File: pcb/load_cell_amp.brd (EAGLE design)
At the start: 50.5 x 30.5 mm, 6 parts, among them IC2 INA122P, J1 LOAD_CELL, J2 G29

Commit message: renamed IC2 to IC1
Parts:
- moved R_REF 1.65 mm to (58.0, 40.6)
- renumbered IC2 to IC1
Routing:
- net N$6: track 10.6 -> 8.93 mm
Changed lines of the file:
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@@
 <text x="34.544" y="46.99" size="1.27" layer="25">V+</text>
 <text x="34.544" y="43.434" size="1.27" layer="25">V-</text>
-<text x="62.23" y="43.18" size="1.27" layer="25">BRAKE</text>
+<text x="61.468" y="43.18" size="1.27" layer="25">BRAKE</text>
 </plain>
 <attributes>
@@
 <attribute name="VALUE" x="41.148" y="49.276" size="1.27" layer="27" ratio="10"/>
 </element>
-<element name="R_REF" library="pot" library_urn="urn:adsk.eagle:library:331" package="RJ9W" package3d_urn="urn:adsk.eagle:package:22702/1" value="2k" x="59.69" y="40.64" smashed="yes" rot="R90">
-<attribute name="NAME" x="57.023" y="36.068" size="1.27" layer="25" ratio="10" rot="R90"/>
-<attribute name="POPULARITY" value="2" x="76.2" y="58.42" size="1.778" layer="27" rot="R90" display="off"/>
-<attribute name="VALUE" x="63.754" y="36.068" size="1.27" layer="27" ratio="10" rot="R90"/>
-</element>
-<element name="IC2" library="g29_load_cell" package="DIL08" package3d_urn="urn:adsk.eagle:package:4906/1" value="INA122P" x="45.72" y="41.91" smashed="yes" rot="R270">
+<element name="R_REF" library="pot" library_urn="urn:adsk.eagle:library:331" package="RJ9W" package3d_urn="urn:adsk.eagle:package:22702/1" value="2k" x="58.039" y="40.64" smashed="yes" rot="R90">
+<attribute name="NAME" x="55.372" y="36.068" size="1.27" layer="25" ratio="10" rot="R90"/>
+<attribute name="POPULARITY" value="2" x="74.549" y="58.42" size="1.778" layer="27" rot="R90" display="off"/>
+<attribute name="VALUE" x="62.103" y="36.068" size="1.27" layer="27" ratio="10" rot="R90"/>
+</element>
+<element name="IC1" library="g29_load_cell" package="DIL08" package3d_urn="urn:adsk.eagle:package:4906/1" value="INA122P" x="45.72" y="41.91" smashed="yes" rot="R270">
 <attribute name="MF" value="TEXAS INSTRUMENTS" x="45.72" y="41.91" size="1.778" layer="27" rot="R270" display="off"/>
 <attribute name="MPN" value="INA122P" x="45.72" y="41.91" size="1.778" layer="27" rot="R270" display="off"/>
@@
 <contactref element="R_GAIN" pad="A"/>
 <wire x1="48.26" y1="53.975" x2="48.26" y2="46.99" width="0.4064" layer="16"/>
-<contactref element="IC2" pad="8"/>
+<contactref element="IC1" pad="8"/>
 <wire x1="48.26" y1="46.99" x2="49.53" y2="45.72" width="0.4064" layer="16"/>
 </signal>
@@
 <wire x1="45.72" y1="53.975" x2="45.72" y2="53.34" width="0.4064" layer="16"/>
 <wire x1="45.72" y1="53.34" x2="41.91" y2="49.53" width="0.4064" layer="16"/>
-<contactref element="IC2" pad="1"/>
+<contactref element="IC1" pad="1"/>
 <wire x1="41.91" y1="49.53" x2="41.91" y2="45.72" width="0.4064" layer="16"/>
 </signal>
@@
 <vertex x="25.4" y="59.69"/>
 </polygon>
-<contactref element="IC2" pad="4"/>
+<contactref element="IC1" pad="4"/>
 </signal>
 <signal name="3.3V">
@@
 <wire x1="40.767" y1="44.45" x2="48.26" y2="44.45" width="0.4064" layer="16"/>
 <wire x1="46.99" y1="33.782" x2="46.99" y2="40.64" width="0.4064" layer="16"/>
-<wire x1="59.055" y1="43.18" x2="63.5" y2="43.18" width="0.4064" layer="16"/>
+<wire x1="57.404" y1="43.18" x2="63.5" y2="43.18" width="0.4064" layer="16"/>
 <wire x1="63.5" y1="43.18" x2="71.12" y2="50.8" width="0.4064" layer="16"/>
-<contactref element="IC2" pad="7"/>
+<contactref element="IC1" pad="7"/>
 <wire x1="46.99" y1="40.64" x2="49.53" y2="43.18" width="0.4064" layer="16"/>
 <wire x1="48.26" y1="44.45" x2="49.53" y2="43.18" width="0.4064" layer="16"/>
-<wire x1="49.53" y1="43.18" x2="59.055" y2="43.18" width="0.4064" layer="16"/>
+<wire x1="49.53" y1="43.18" x2="57.404" y2="43.18" width="0.4064" layer="16"/>
 </signal>
 <signal name="N$6">
 <contactref element="R_REF" pad="S"/>
-<wire x1="59.055" y1="40.64" x2="54.61" y2="40.64" width="0.4064" layer="16"/>
+<wire x1="57.404" y1="40.64" x2="54.61" y2="40.64" width="0.4064" layer="16"/>
 <wire x1="54.61" y1="40.64" x2="52.07" y2="38.1" width="0.4064" layer="16"/>
-<contactref element="IC2" pad="5"/>
+<contactref element="IC1" pad="5"/>
 <wire x1="52.07" y1="38.1" x2="49.53" y2="38.1" width="0.4064" layer="16"/>
 </signal>
@@
 <wire x1="67.1806375" y1="43.8" x2="65.2906375" y2="41.91" width="0.4064" layer="16"/>
 <wire x1="65.2906375" y1="41.91" x2="50.8" y2="41.91" width="0.4064" layer="16"/>
-<contactref element="IC2" pad="6"/>
+<contactref element="IC1" pad="6"/>
 <wire x1="50.8" y1="41.91" x2="49.53" y2="40.64" width="0.4064" layer="16"/>
 </signal>
@@
 <wire x1="30.48" y1="44.14" x2="30.79" y2="44.14" width="0.4064" layer="16"/>
 <wire x1="30.79" y1="44.14" x2="34.29" y2="40.64" width="0.4064" layer="16"/>
-<contactref element="IC2" pad="3"/>
+<contactref element="IC1" pad="3"/>
 <wire x1="34.29" y1="40.64" x2="41.91" y2="40.64" width="0.4064" layer="16"/>
 </signal>
@@
 <wire x1="30.48" y1="47.64" x2="32.37" y2="47.64" width="0.4064" layer="16"/>
 <wire x1="32.37" y1="47.64" x2="36.83" y2="43.18" width="0.4064" layer="16"/>
-<contactref element="IC2" pad="2"/>
+<contactref element="IC1" pad="2"/>
 <wire x1="36.83" y1="43.18" x2="41.91" y2="43.18" width="0.4064" layer="16"/>
 </signal>

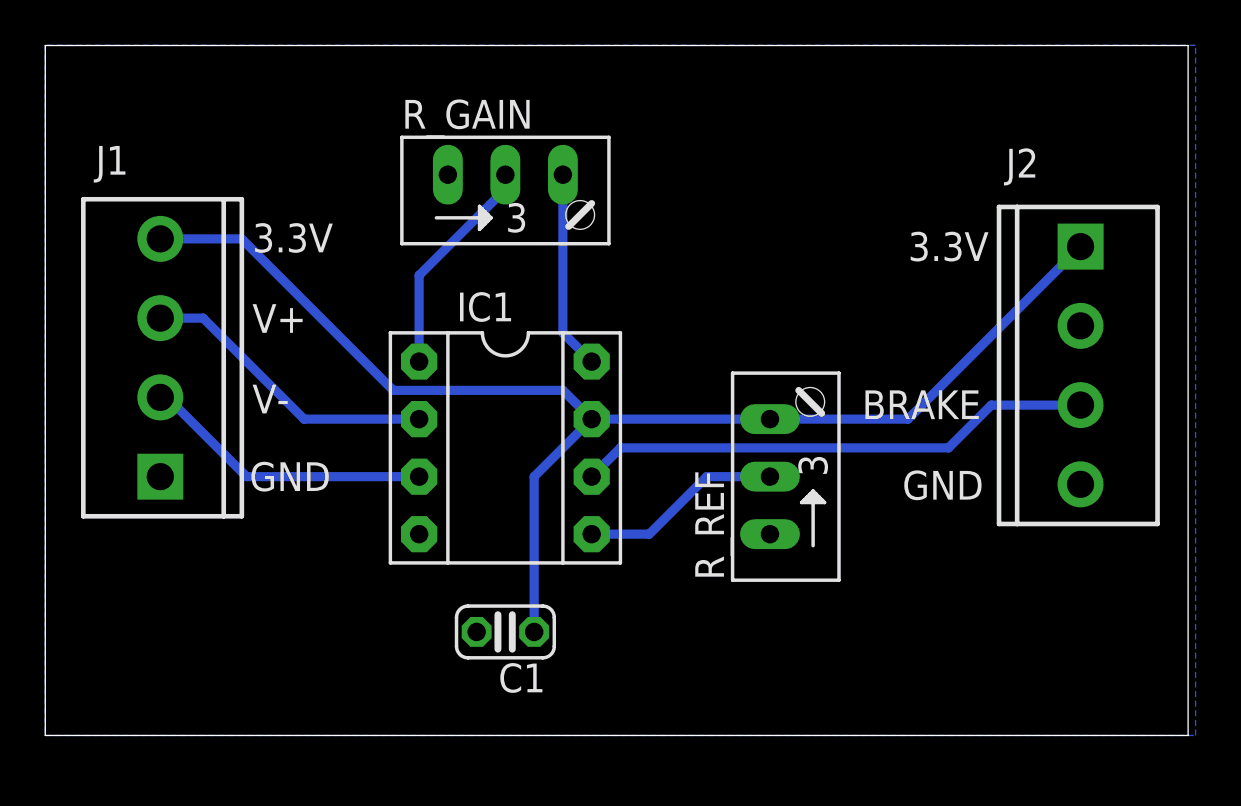
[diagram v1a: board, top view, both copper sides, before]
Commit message: updated schematic to support single cell
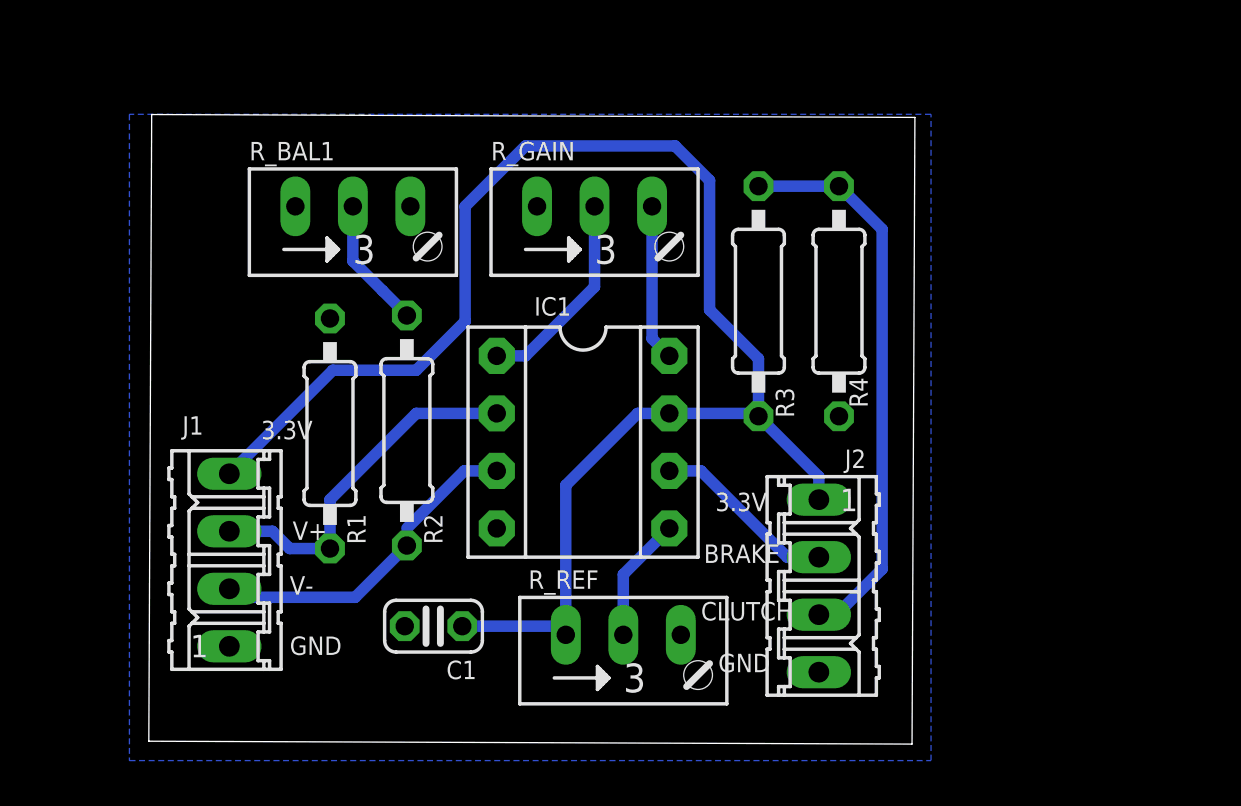
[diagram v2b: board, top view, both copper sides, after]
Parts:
- added R1, R2, R3: 1k, rcl:0207/10
- added R4: 9k, rcl:0207/10
- added R_BAL1: 10, pot:RJ9W
- J1, J2: device SparkFun-Connectors:SCREWTERMINAL-3.5MM-4 -> con-amp-quick:04P
- moved J2 18.9 mm to (59.6, 35.8)
- moved R_REF 10.4 mm to (50.9, 33.0), turned to 0 degrees
- moved J1 4.78 mm to (33.5, 37.0)
- moved R_GAIN 4.18 mm to (49.7, 51.9)
- moved IC1 3.44 mm to (49.1, 42.2)
- moved C1 3.19 mm to (42.5, 34.0)
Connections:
- removed net N$7: IC1.6, J2.3
- new net CLUTCH: IC1.6, J2.2
- new net N$5: R2.1, R_BAL1.S
- new net N$9: J2.3, R3.1, R4.2
- net 3.3V: now also R3.2, R_REF.E; no longer R_REF.A
- net GND: now also R1.1, R4.1, R_BAL1.E, R_REF.A; no longer R_REF.E
- net N$3: now also R2.2
- net N$4: now also R1.2
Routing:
- net N$9: track 0.00 -> 24.9 mm
- net N$7: track 22.9 -> 0.00 mm
- net 3.3V: track 57.5 -> 68.0 mm
- net CLUTCH: track 0.00 -> 8.18 mm
- net N$5: track 0.00 -> 5.81 mm
- net N$6: track 8.93 -> 5.54 mm
- net N$4: track 13.3 -> 15.9 mm
- net N$1: track 8.78 -> 6.92 mm
- net N$3: track 12.9 -> 14.7 mm
- net N$2: track 9.83 -> 9.14 mm
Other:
- board size 50.5 x 30.5 mm -> 33.8 x 27.8 mm
- board text added: "CLUTCH"
